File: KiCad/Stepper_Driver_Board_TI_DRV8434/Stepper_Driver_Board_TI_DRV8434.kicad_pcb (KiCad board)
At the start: 4 copper layers, 75 x 46.8 mm, 25 parts, among them J1 Motor Connect, J2 PWR & DATA Connect, J3 Battery Connect, SW1 SW_SPDT_MSM, SW2 SW_SPDT_MSM, U1 DRV8434PWPR, U2 PC817, U4 6N137, U6 PC817

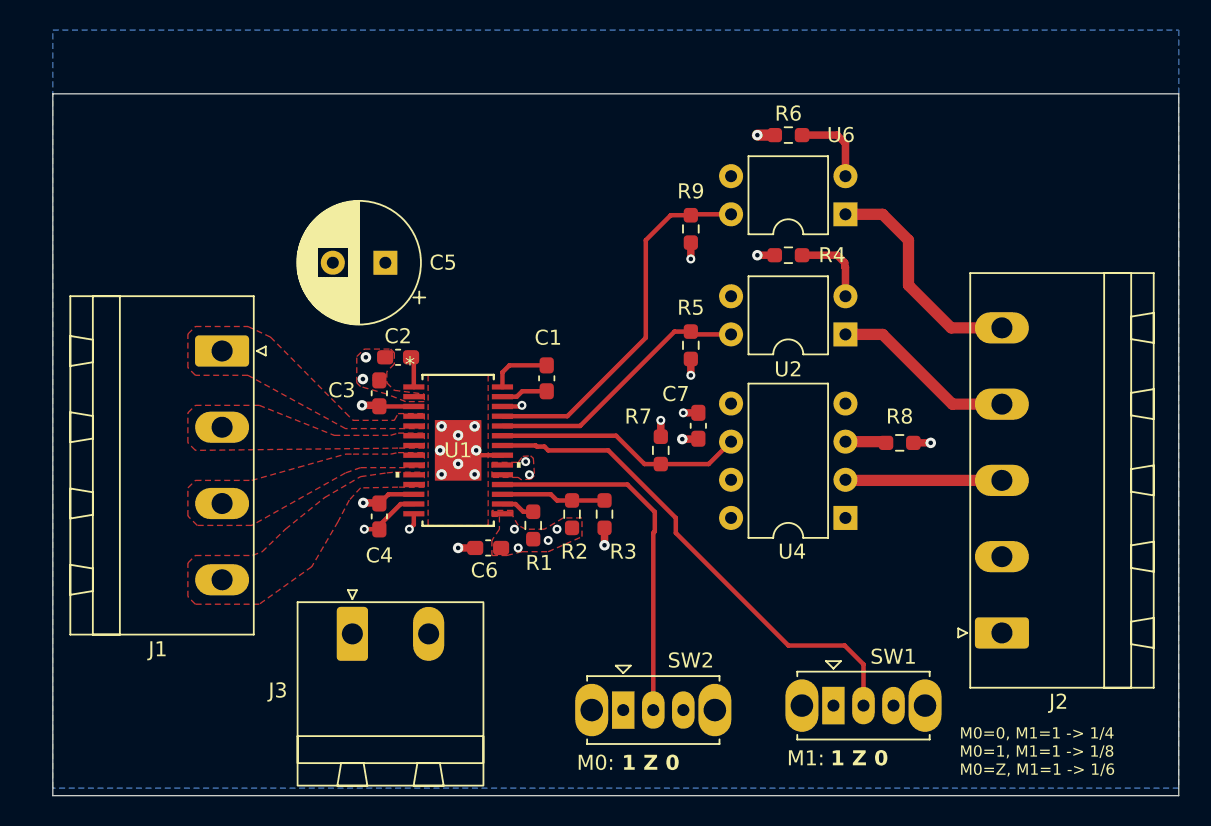
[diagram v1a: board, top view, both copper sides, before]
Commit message: Added Ground Plane and stiching vias
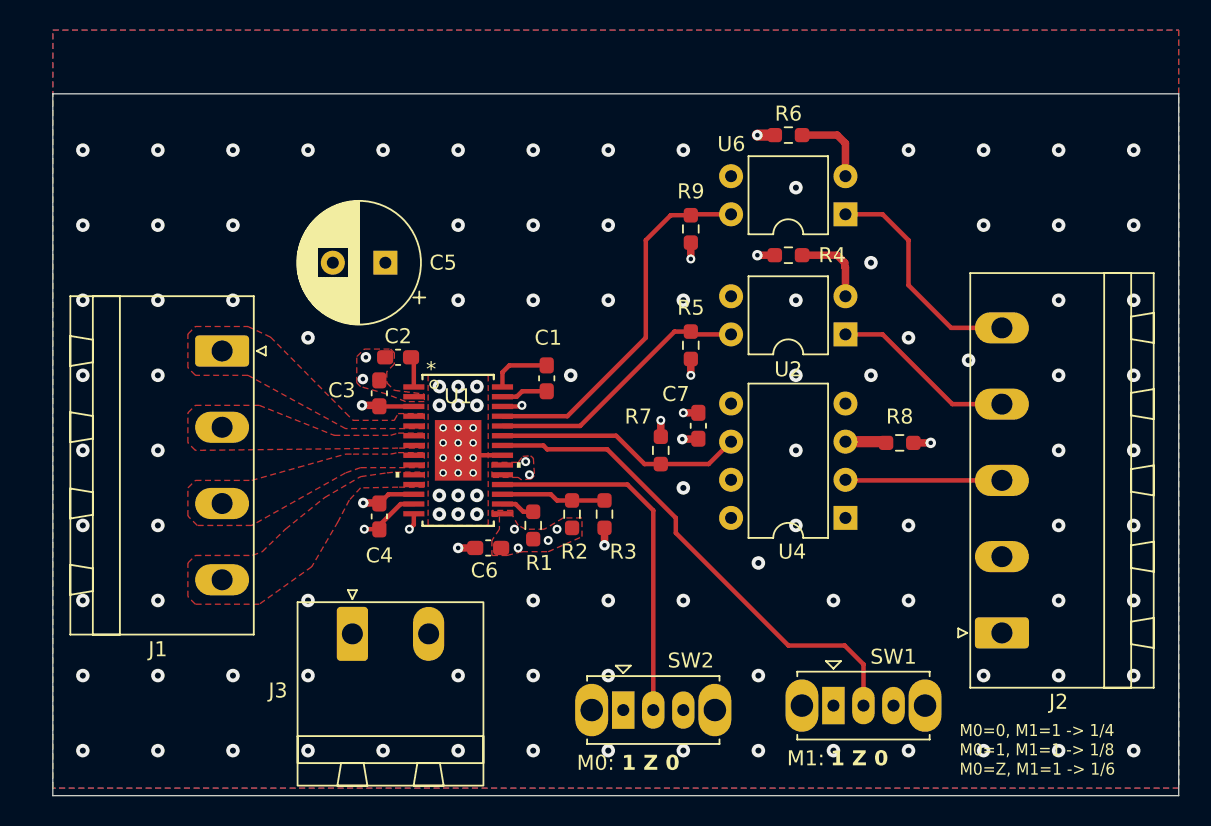
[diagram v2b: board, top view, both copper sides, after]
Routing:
- net +BATT: track 5.46 -> 4.44 mm
- net GND: vias 17 -> 126

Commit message: Needs some more work on 2esp
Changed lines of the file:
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@@
 		(layer "F.Cu")
 		(at 175.8 79.5 180)
-		(descr "8-lead though-hole mounted DIP package, row spacing 7.62 mm (300 mils)")
+		(descr "8-lead though-hole mounted DIP package, row spacing 7.62mm (300 mils)")
 		(tags "THT DIP DIL PDIP 2.54mm 7.62mm 300mil")
 		(property "Reference" "U4"
@@
 			(layer "F.SilkS")
 		)
-		(fp_line
-			(start 8.7 9.15)
-			(end 8.7 -1.55)
+		(fp_rect
+			(start -1.06 -1.52)
+			(end 8.67 9.14)
 			(stroke
 				(width 0.05)
 				(type solid)
 			)
-			(layer "F.CrtYd")
-		)
-		(fp_line
-			(start 8.7 -1.55)
-			(end -1.1 -1.55)
-			(stroke
-				(width 0.05)
-				(type solid)
-			)
-			(layer "F.CrtYd")
-		)
-		(fp_line
-			(start -1.1 9.15)
-			(end 8.7 9.15)
-			(stroke
-				(width 0.05)
-				(type solid)
-			)
-			(layer "F.CrtYd")
-		)
-		(fp_line
-			(start -1.1 -1.55)
-			(end -1.1 9.15)
-			(stroke
-				(width 0.05)
-				(type solid)
-			)
+			(fill no)
 			(layer "F.CrtYd")
 		)
@@
 			)
 		)
-		(pad "1" thru_hole rect
+		(pad "1" thru_hole roundrect
 			(at 0 0 180)
 			(size 1.6 1.6)
@@
 			(layers "*.Cu" "*.Mask")
 			(remove_unused_layers no)
+			(roundrect_rratio 0.15625)
 			(net 25 "unconnected-(U4-NC-Pad1)")
 			(pinfunction "NC")
 			(pintype "passive+no_connect")
 		)
-		(pad "2" thru_hole oval
+		(pad "2" thru_hole circle
 			(at 0 2.54 180)
 			(size 1.6 1.6)
@@
 			(pintype "passive")
 		)
-		(pad "3" thru_hole oval
+		(pad "3" thru_hole circle
 			(at 0 5.08 180)
 			(size 1.6 1.6)
@@
 			(pintype "passive")
 		)
-		(pad "4" thru_hole oval
+		(pad "4" thru_hole circle
 			(at 0 7.62 180)
 			(size 1.6 1.6)
@@
 			(pintype "passive+no_connect")
 		)
-		(pad "5" thru_hole oval
+		(pad "5" thru_hole circle
 			(at 7.62 7.62 180)
 			(size 1.6 1.6)
@@
 			(pintype "power_in")
 		)
-		(pad "6" thru_hole oval
+		(pad "6" thru_hole circle
 			(at 7.62 5.08 180)
 			(size 1.6 1.6)
@@
 			(pintype "open_collector")
 		)
-		(pad "7" thru_hole oval
+		(pad "7" thru_hole circle
 			(at 7.62 2.54 180)
 			(size 1.6 1.6)
@@
 			(pintype "input+no_connect")
 		)
-		(pad "8" thru_hole oval
+		(pad "8" thru_hole circle
 			(at 7.62 0 180)
 			(size 1.6 1.6)
@@
 		)
 		(embedded_fonts no)
-		(model "${KICAD8_3DMODEL_DIR}/Package_DIP.3dshapes/DIP-8_W7.62mm.wrl"
+		(model "${KICAD9_3DMODEL_DIR}/Package_DIP.3dshapes/DIP-8_W7.62mm.step"
 			(offset
 				(xyz 0 0 0)

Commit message: Final KiCad stuff for 2ESP and Driver Board
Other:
- board text added: "NEON CARROT STEPPER MOTOR DRIVER"
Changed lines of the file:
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@@
 			(drillshape 0)
 			(scaleselection 1)
-			(outputdirectory "/Users/phennessey/Desktop/")
+			(outputdirectory "/Users/phennessey/Desktop/GerberDump/")
 		)
 	)
@@
 		)
 	)
+	(gr_text "NEON CARROT\nSTEPPER MOTOR DRIVER"
+		(at 143.282651 58 0)
+		(layer "F.SilkS")
+		(effects
+			(font
+				(size 2 2)
+				(thickness 0.4)
+				(bold yes)
+			)
+			(justify bottom)
+		)
+	)
 	(gr_text "M1:"
 		(at 171.9 96.1 0)
@@
 	)
 	(zone
+		(net 0)
+		(net_name "")
+		(layer "F.Cu")
+		(hatch edge 0.5)
+		(connect_pads
+			(clearance 0)
+		)
+		(min_thickness 0.25)
+		(filled_areas_thickness no)
+		(keepout
+			(tracks allowed)
+			(vias allowed)
+			(pads allowed)
+			(copperpour not_allowed)
+			(footprints allowed)
+		)
+		(placement
+			(enabled no)
+			(sheetname "/")
+		)
+		(fill
+			(thermal_gap 0.5)
+			(thermal_bridge_width 0.5)
+		)
+		(polygon
+			(pts
+				(xy 145.6 78.1) (xy 145.95 78.1) (xy 145.95 78.3) (xy 145.6 78.3)
+			)
+		)
+	)
+	(zone
 		(net 5)
 		(net_name "GND")
@@
 		(polygon
 			(pts
-				(xy 123 47) (xy 198 47) (xy 198 97.5) (xy 123 97.5)
+				(xy 123 50.8) (xy 198.12 50.8) (xy 198 97.5) (xy 123 97.5)
 			)
 		)
@@
 		(hatch edge 0.5)
 		(priority 1)
-		(connect_pads
+		(connect_pads yes
 			(clearance 0.5)
 		)
@@
 		(fill yes
 			(thermal_gap 0.5)
-			(thermal_bridge_width 0.5)
+			(thermal_bridge_width 0.75)
 		)
 		(polygon
